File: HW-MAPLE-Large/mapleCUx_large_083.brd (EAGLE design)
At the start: 100 x 59 mm, 56 parts, among them IC1 DS2482, IC2 LAN-USR-ES1, Q1 BSS84, X4 1751248, X7 1751264

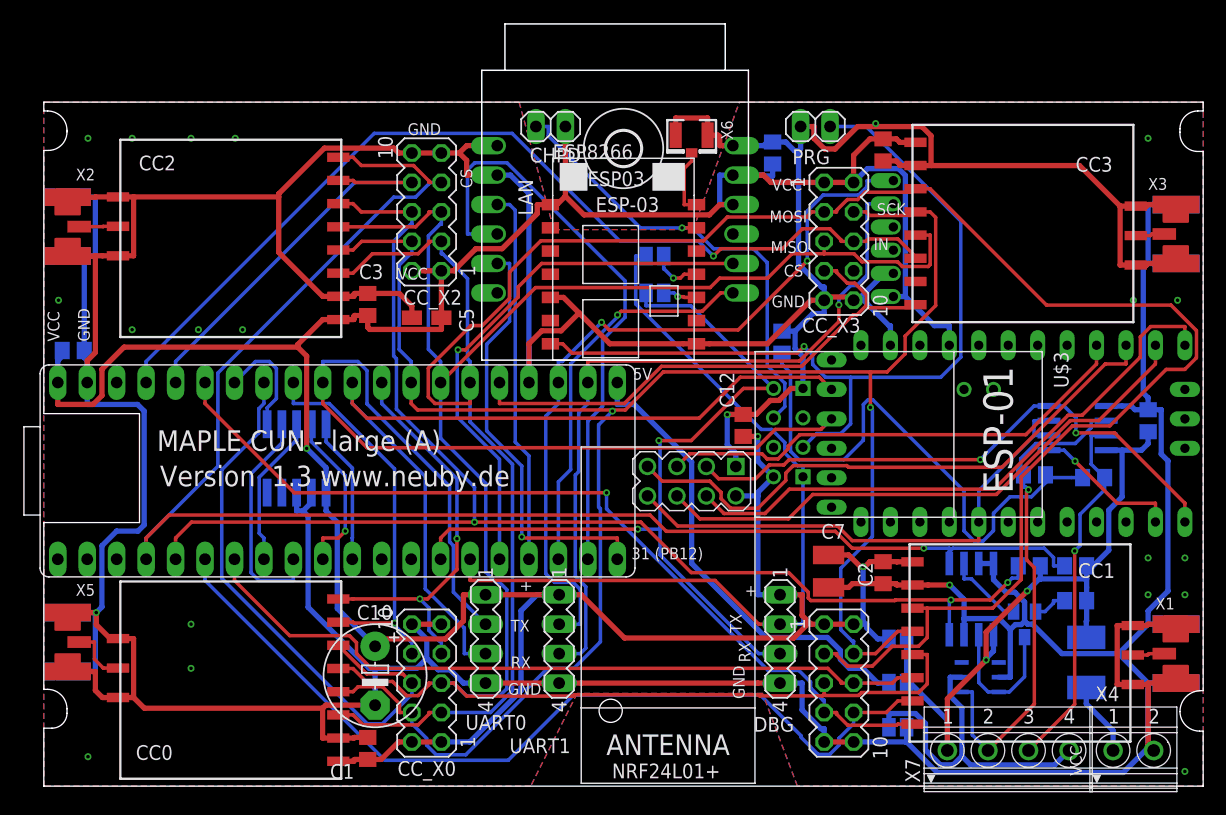
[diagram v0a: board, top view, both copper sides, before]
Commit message: Large 083 Antennas rerouted
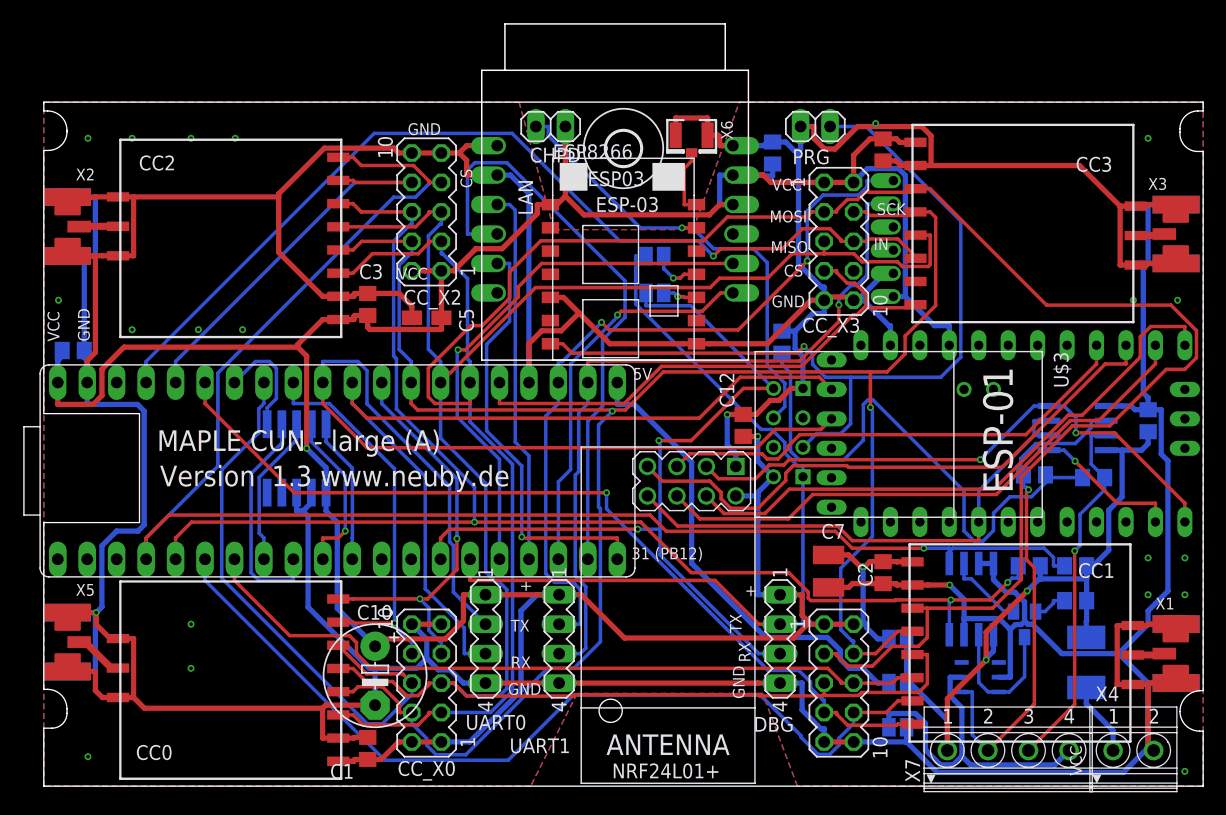
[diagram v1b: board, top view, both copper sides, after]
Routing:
- net N$4: track 5.15 -> 4.30 mm
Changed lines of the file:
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@@
 <contactref element="CC0" pad="ANT"/>
 <contactref element="X5" pad="P"/>
-<wire x1="6.4" y1="10.185" x2="5.1299" y2="10.185" width="0.3048" layer="1"/>
-<wire x1="3.048" y1="12.43" x2="4.3689" y2="12.43" width="0.3048" layer="1"/>
-<wire x1="4.3689" y1="12.43" x2="4.3689" y2="10.946" width="0.3048" layer="1"/>
-<wire x1="4.3689" y1="10.946" x2="5.1299" y2="10.185" width="0.3048" layer="1"/>
+<wire x1="6.4" y1="10.185" x2="5.817" y2="10.185" width="0.6096" layer="1"/>
+<wire x1="5.817" y1="10.185" x2="3.556" y2="12.446" width="0.6096" layer="1"/>
+<wire x1="3.556" y1="12.446" x2="3.064" y2="12.446" width="0.6096" layer="1"/>
+<wire x1="3.064" y1="12.446" x2="3.048" y2="12.43" width="0.6096" layer="1"/>
 </signal>
 <signal name="N$1">
 <contactref element="CC1" pad="ANT"/>
 <contactref element="X1" pad="P"/>
-<wire x1="93.93" y1="11.31" x2="95.2001" y2="11.31" width="0.3048" layer="1"/>
-<wire x1="96.647" y1="11.43" x2="95.3201" y2="11.43" width="0.3048" layer="1"/>
-<wire x1="95.3201" y1="11.43" x2="95.2001" y2="11.31" width="0.3048" layer="1"/>
+<wire x1="93.93" y1="11.31" x2="96.527" y2="11.31" width="0.6096" layer="1"/>
+<wire x1="96.527" y1="11.31" x2="96.647" y2="11.43" width="0.6096" layer="1"/>
 </signal>
 <signal name="N$3">
 <contactref element="X2" pad="P"/>
 <contactref element="CC2" pad="ANT"/>
-<wire x1="6.4" y1="48.285" x2="5.1299" y2="48.285" width="0.3048" layer="1"/>
-<wire x1="3.048" y1="48.26" x2="5.1049" y2="48.26" width="0.3048" layer="1"/>
-<wire x1="5.1049" y1="48.26" x2="5.1299" y2="48.285" width="0.3048" layer="1"/>
+<wire x1="6.4" y1="48.285" x2="3.048" y2="48.285" width="0.6096" layer="1"/>
+<wire x1="3.048" y1="48.285" x2="3.048" y2="48.26" width="0.6096" layer="1"/>
 </signal>
 <signal name="N$2">
 <contactref element="CC4" pad="ANT"/>
 <contactref element="X3" pad="P"/>
-<wire x1="94.184" y1="47.489" x2="95.4541" y2="47.489" width="0.3048" layer="1"/>
-<wire x1="96.647" y1="47.625" x2="95.5901" y2="47.625" width="0.3048" layer="1"/>
-<wire x1="95.5901" y1="47.625" x2="95.4541" y2="47.489" width="0.3048" layer="1"/>
+<wire x1="94.184" y1="47.489" x2="96.511" y2="47.489" width="0.6096" layer="1"/>
+<wire x1="96.511" y1="47.489" x2="96.647" y2="47.625" width="0.6096" layer="1"/>
 </signal>
 <signal name="VDD" class="1">
